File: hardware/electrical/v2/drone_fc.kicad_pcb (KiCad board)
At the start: 4 copper layers, 30 x 40.8 mm, 37 parts, among them J1 Cortex_SWD_10P, J2 ESC_4IN1_JST_SH, U1 TLV75533PDBVR, U2 LMR50410_Buck, U3 MDBT53-P1M, U4 ICM-42688-P

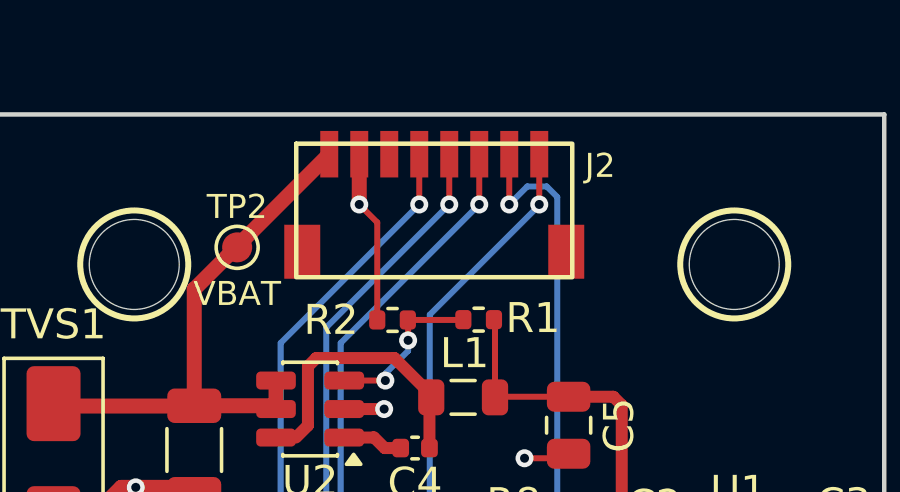
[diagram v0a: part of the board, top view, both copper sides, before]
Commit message: j2: adopt the KiCad library footprint for the ESC connector
Switches J2 from the hand-made drone_fc_v2_footprints copy to KiCad's
Connector_JST:JST_SH_SM08B-SRSS-TB_1x08-1MP_P1.00mm_Horizontal.

The two disagreed on the mechanical retention pads: signal-to-MP separation
of 3.25 mm against 3.875 mm, with the MP pads 0.4 mm further out in the
library version. Those pads take the load every time the ESC harness is
unplugged, so the geometry matters. JST's own drawing could not be read
programmatically to arbitrate, but provenance is decisive - the library
footprint is machine-generated from eSH.pdf by kicad-footprint-generator and
peer-reviewed, whereas ours came from the same CopperPilot generation that
produced mislabelled symbol pins, a self-intersecting courtyard and an
unverified BOM. The swap also brings the manufacturer STEP model, which the
custom footprint lacked.

Also links TP1-TP4 to their schematic symbols. Those pads were created
directly in the board file before the matching TestPoint symbols existed, so
they carried no path and Update PCB from Schematic kept offering to add four
duplicates.

This is an intermediate state with known errors. Fitting the reviewed
footprint revealed that the connector opens toward the board centre rather
than out through the edge, so it still needs rotating 180 degrees and moving
to y ~88.6. Until then DRC reports eight board-edge clearance errors (pads
0.425 mm from the edge against a 0.5 mm rule) and a courtyard overlap with
TP2, all within the area that rework will cover. ERC is clean and no nets
are unconnected.
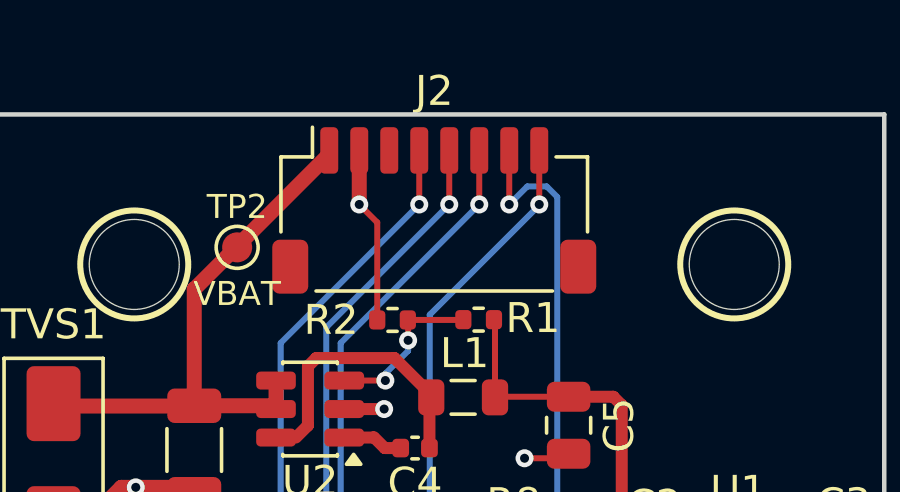
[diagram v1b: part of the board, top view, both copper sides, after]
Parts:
- J2: footprint drone_fc_v2_footprints:JST_SH_SM08B-SRSS-TB_1x08-1MP_P1.00mm_Horizontal -> Connector_JST:JST_SH_SM08B-SRSS-TB_1x08-1MP_P1.00mm_Horizontal

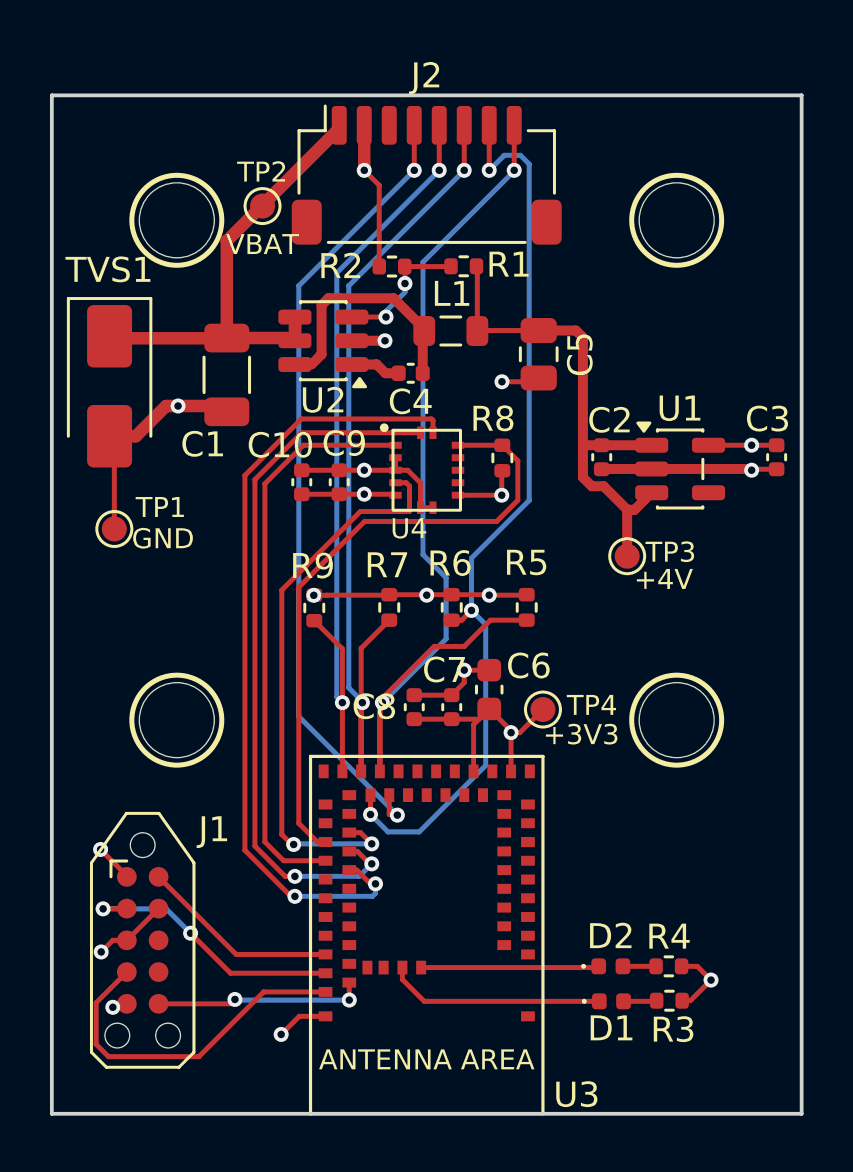
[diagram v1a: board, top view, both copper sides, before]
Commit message: j2: reverse connector pin numbering to match the ESC harness
The board-side pinout is now pin 1 = M4 through pin 8 = VBAT, reversed from
the JST convention the parts-list documents. This matches the custom harness
as measured: with the socket held open-end toward you, VBAT sits on the right,
which places it on the left-hand pad once the header is rotated to open
outward. Pin numbering is reversed in the symbol rather than the footprint, so
the schematic drawing and its wiring are unchanged and only the pad mapping
moves.

J2 is rotated 180 degrees so the connector opens out through the top board
edge rather than into the board interior. The opening direction was settled by
rendering the manufacturer STEP model - the 2D pads and courtyard are
ambiguous, and reasoning from them produced two wrong conclusions before the
render.

Intermediate state. Re-routing around the rotated connector is unfinished:
three nets are open in the buck area (+4V, C5 ground, R2 feedback) and both J2
mounting pads sit 0.235 mm from the board edge against a 0.5 mm rule, so the
connector needs nudging inboard. ERC is clean and the remaining twelve DRC
findings are silkscreen only.

Committed mid-edit because KiCad crashed; the files were checked for damage
first and both parse cleanly.
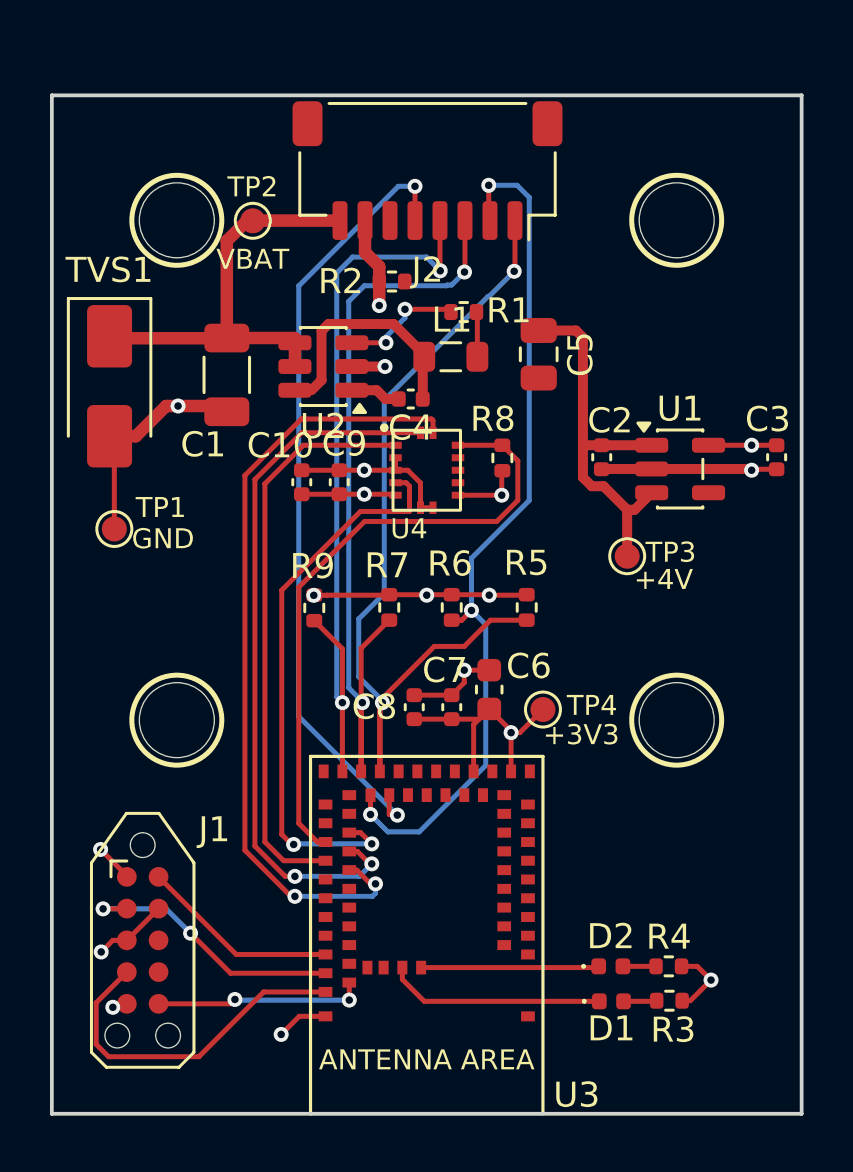
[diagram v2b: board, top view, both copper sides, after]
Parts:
- moved R1 1.83 mm to (101.5, 93.7)
- moved C4 1.03 mm to (99.4, 97.2)
- moved U2 1.03 mm to (95.9, 95.8)
- moved L1 1.03 mm to (101.0, 95.5)
- moved TP2 0.71 mm to (93.0, 90.0)
- moved R2 0.60 mm to (98.6, 92.5)
- moved J2 0.19 mm to (100.0, 88.0), turned to 180 degrees
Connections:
- J2 pad 1: /VBAT -> /ESC_M4
- J2 pad 2: GND -> /ESC_M3
- J2 pad 3: unconnected-(J2-CURRENT-Pad3) -> /ESC_M2
- J2 pad 4: /ESC_TLM -> /ESC_M1
- J2 pad 5: /ESC_M1 -> /ESC_TLM
- J2 pad 6: /ESC_M2 -> unconnected-(J2-CURRENT-Pad6)
- J2 pad 7: /ESC_M3 -> GND
- J2 pad 8: /ESC_M4 -> /VBAT
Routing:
- net GND: track 52.3 -> 48.6 mm, vias 14 -> 13
- net /ESC_M4: track 38.6 -> 35.1 mm
- net /+4V: track 20.7 -> 17.4 mm
- net /ESC_M3: track 36.5 -> 34.8 mm
- net /VBAT: track 16.5 -> 15.0 mm
- net /ESC_M2: track 34.3 -> 32.8 mm
- net Net-(U2-FB): track 5.73 -> 4.95 mm
- net /ESC_M1: track 31.2 -> 30.4 mm

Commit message: j2: clear the connector mounting pads from the board edge
Moves J2 to y=88.3, putting its mounting pads 0.525 mm from the board edge
against the 0.5 mm rule. The rotation to open outward had left them at
0.235 mm. Re-routing around the rotated connector is finished.

The board is now electrically complete: ERC clean, every net routed, and no
copper, clearance, short, drill or board-edge violations. The four remaining
DRC findings are silkscreen only and accepted - the U3 outline is clipped by
the board edge because the module is deliberately edge-aligned for its
antenna, and the U4 outline crosses its own pads in the footprint itself.
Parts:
- moved TP2 0.42 mm to (93.3, 90.3)
- moved J2 0.29 mm to (100.0, 88.3)
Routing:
- net /+4V: track 17.4 -> 20.2 mm
- net GND: track 48.6 -> 49.9 mm, vias 13 -> 14
- net Net-(U2-FB): track 4.95 -> 6.07 mm
